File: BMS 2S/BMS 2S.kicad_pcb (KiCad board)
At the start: 2 copper layers, 20 parts

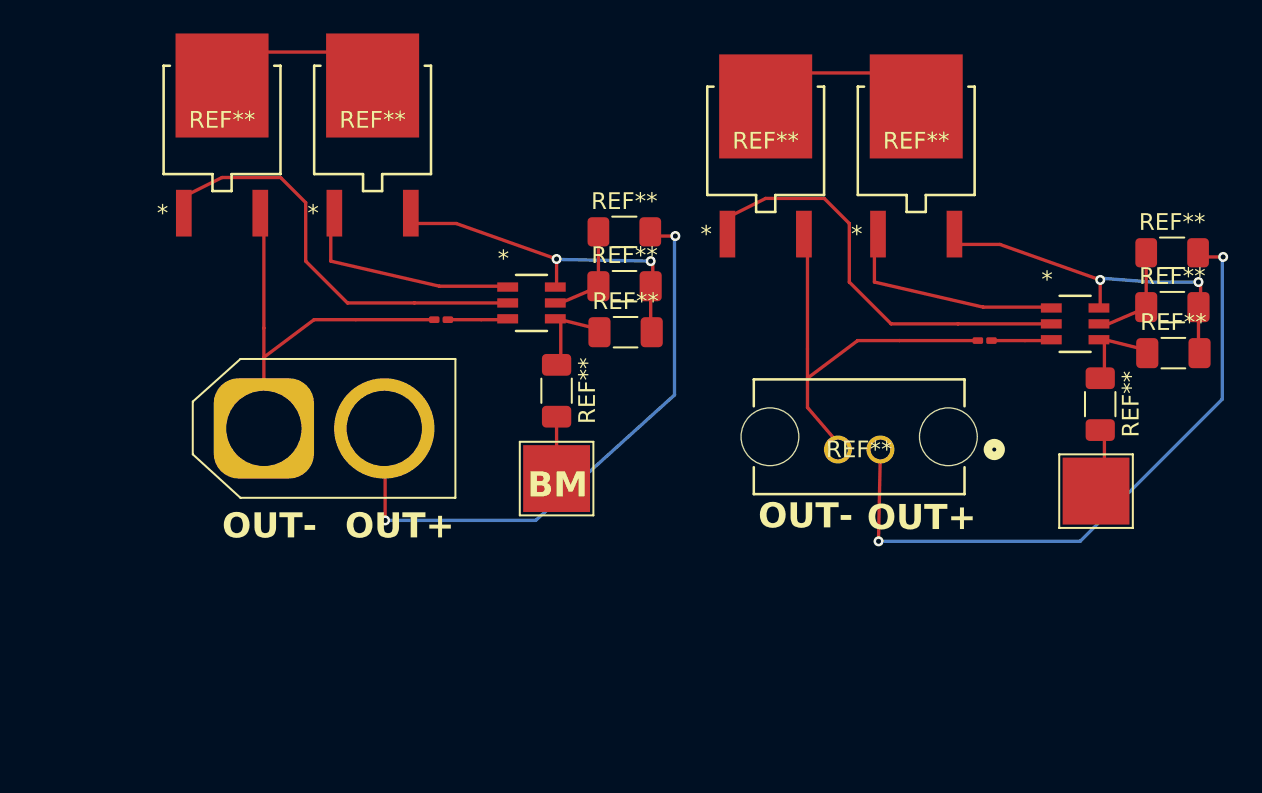
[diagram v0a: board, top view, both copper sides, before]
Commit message: Nouvelle itération du bms
Quelques bugs de connection a régler entre les power planes et les R,C et Screws terminals, + vérifications
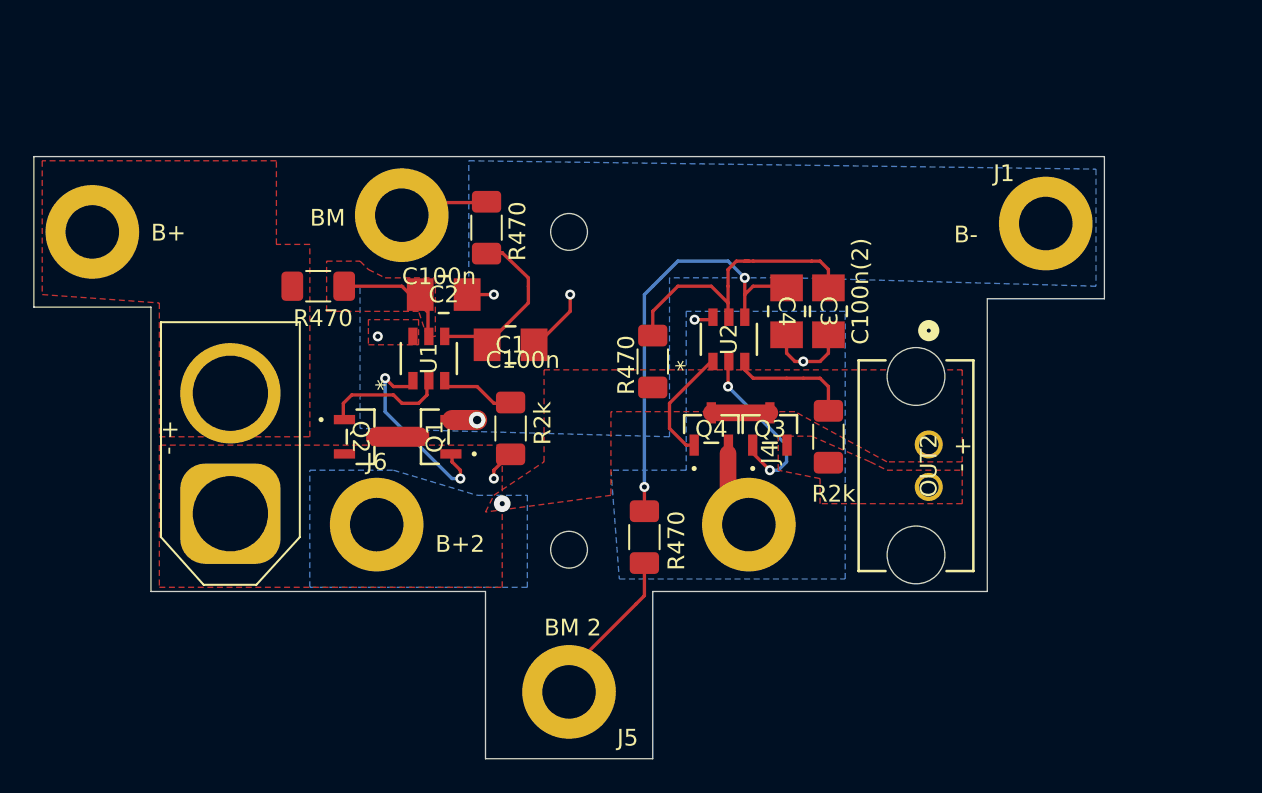
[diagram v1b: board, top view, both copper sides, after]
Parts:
- removed B+/-: AMASS_XT60-M_1x02_P7.20mm_Vertical, Connector_AMASS:AMASS_XT60-M_1x02_P7.20mm_Vertical
- removed the REF** at (142.1, 79.0)
- removed the REF** at (142.1, 85.0)
- removed the REF** at (136.2, 83.2)
- removed the REF** at (109.4, 83.8)
- removed the REF** at (137.8, 88.0)
- removed the REF** at (142.1, 82.2)
- removed the REF** at (85.2, 71.1)
- removed the REF** at (117.8, 72.3)
- removed the REF** at (94.2, 71.1)
- removed the REF** at (130.8, 84.2)
- removed the REF** at (105.2, 87.2)
- removed the REF** at (105.2, 92.5)
- removed the REF** at (137.5, 93.2)
- removed the REF** at (103.8, 82.0)
- removed the REF** at (109.3, 81.0)
- removed the REF** at (124.6, 90.8)
- removed the REF** at (109.3, 77.8)
- removed the REF** at (126.8, 72.3)
- removed the REF** at (98.3, 83.0)
- added C1: 1206cap, BMS_footprints:1206cap, F.Cu at (102.5, 84.5)
- added C2: 1206cap, BMS_footprints:1206cap, F.Cu at (98.5, 81.5)
- added C3: 1206cap, BMS_footprints:1206cap, F.Cu at (121.5, 82.5)
- added C4: 1206cap, BMS_footprints:1206cap, F.Cu at (119.0, 82.5)
- added J1: MountingHole_3.2mm_M3_DIN965_Pad, MountingHole:MountingHole_3.2mm_M3_DIN965_Pad, F.Cu at (134.5, 77.3)
- added J2: MountingHole_3.2mm_M3_DIN965_Pad, MountingHole:MountingHole_3.2mm_M3_DIN965_Pad, F.Cu at (96.0, 76.8)
- added J3: MountingHole_3.2mm_M3_DIN965_Pad, MountingHole:MountingHole_3.2mm_M3_DIN965_Pad, F.Cu at (77.5, 77.8)
- added J4: MountingHole_3.2mm_M3_DIN965_Pad, MountingHole:MountingHole_3.2mm_M3_DIN965_Pad, F.Cu at (116.7, 95.3)
- added J5: MountingHole_3.2mm_M3_DIN965_Pad, MountingHole:MountingHole_3.2mm_M3_DIN965_Pad, F.Cu at (106.0, 105.3)
- added J6: MountingHole_3.2mm_M3_DIN965_Pad, MountingHole:MountingHole_3.2mm_M3_DIN965_Pad, F.Cu at (94.5, 95.3)
- added OUT1: AMASS_XT60-M_1x02_P7.20mm_Vertical, Connector_AMASS:AMASS_XT60-M_1x02_P7.20mm_Vertical, F.Cu at (85.8, 94.6)
- added OUT2: 705450001, BMS_footprints:CONN_70545-xxxx_02_MOL, F.Cu at (127.5, 90.5)
- added Q1: DMG2302UK-7, BMS_footprints:SOT23_DMG230_DIO, F.Cu at (98.0, 90.0)
- added Q2: DMG2302UK-7, BMS_footprints:SOT23_DMG230_DIO, F.Cu at (93.5, 90.0)
- added Q3: DMG2302UK-7, BMS_footprints:SOT23_DMG230_DIO, F.Cu at (118.0, 89.5)
- added Q4: DMG2302UK-7, BMS_footprints:SOT23_DMG230_DIO, F.Cu at (114.5, 89.5)
- added R1: R_1206_3216Metric_Pad1.30x1.75mm_HandSolder, Resistor_SMD:R_1206_3216Metric_Pad1.30x1.75mm_HandSolder, F.Cu at (101.1, 77.5)
- added R2: R_1206_3216Metric_Pad1.30x1.75mm_HandSolder, Resistor_SMD:R_1206_3216Metric_Pad1.30x1.75mm_HandSolder, F.Cu at (91.0, 81.0)
- added R3: R_1206_3216Metric_Pad1.30x1.75mm_HandSolder, Resistor_SMD:R_1206_3216Metric_Pad1.30x1.75mm_HandSolder, F.Cu at (102.5, 89.5)
- added R4: R_1206_3216Metric_Pad1.30x1.75mm_HandSolder, Resistor_SMD:R_1206_3216Metric_Pad1.30x1.75mm_HandSolder, F.Cu at (111.0, 85.5)
- added R5: R_1206_3216Metric_Pad1.30x1.75mm_HandSolder, Resistor_SMD:R_1206_3216Metric_Pad1.30x1.75mm_HandSolder, F.Cu at (110.5, 96.0)
- added R6: R_1206_3216Metric_Pad1.30x1.75mm_HandSolder, Resistor_SMD:R_1206_3216Metric_Pad1.30x1.75mm_HandSolder, F.Cu at (121.5, 90.0)
- added REF**: MountingHole_2.2mm_M2, MountingHole:MountingHole_2.2mm_M2, F.Cu at (106.0, 77.8)
- added REF**: MountingHole_2.2mm_M2, MountingHole:MountingHole_2.2mm_M2, F.Cu at (106.0, 96.8)
- added U1: S-8252AAZ-M6T1U, BMS_footprints:SOT236-A-PKG_MP006-A-P-SD-2.1_ABL, F.Cu at (97.6, 85.3)
- added U2: S-8252AAZ-M6T1U, BMS_footprints:SOT236-A-PKG_MP006-A-P-SD-2.1_ABL, F.Cu at (115.5, 84.2)
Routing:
- net Net-(U2-VC): vias 0 -> 2
- net Net-(Q3-G): vias 0 -> 2
- net Net-(Q1-G): vias 0 -> 2
- net B-2: vias 0 -> 1
- net B-: vias 0 -> 2
- net (no net): vias 8 -> 5
- added copper zone on F.Cu, net (none)
- added copper zone on B.Cu, net B-
- added copper zone on F.Cu, net B-
- added copper zone on B.Cu, net B-2
- added copper zone on F.Cu, net Net-(U1-VDD)
- added copper zone on B.Cu, net Out+ B+2
- added copper zone on F.Cu, net Out+ B+2
- added copper zone on F.Cu, net Out-
- added copper zone on F.Cu, net Out-2
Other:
- board outline added: 64 x 36 mm
- board text added: "+ -"
- board text added: "B+"
- board text added: "B+2"
- board text added: "B-"
- board text added: "BM 2"
- board text added: "C100n"
- board text added: "C100n(2)"
- board text added: "R2k"
- board text added: "R470"
- board text removed: "OUT+"
- board text removed: "OUT-"
- board text removed: "gnd"

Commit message: BMS- Réglage des bugs de link power plane
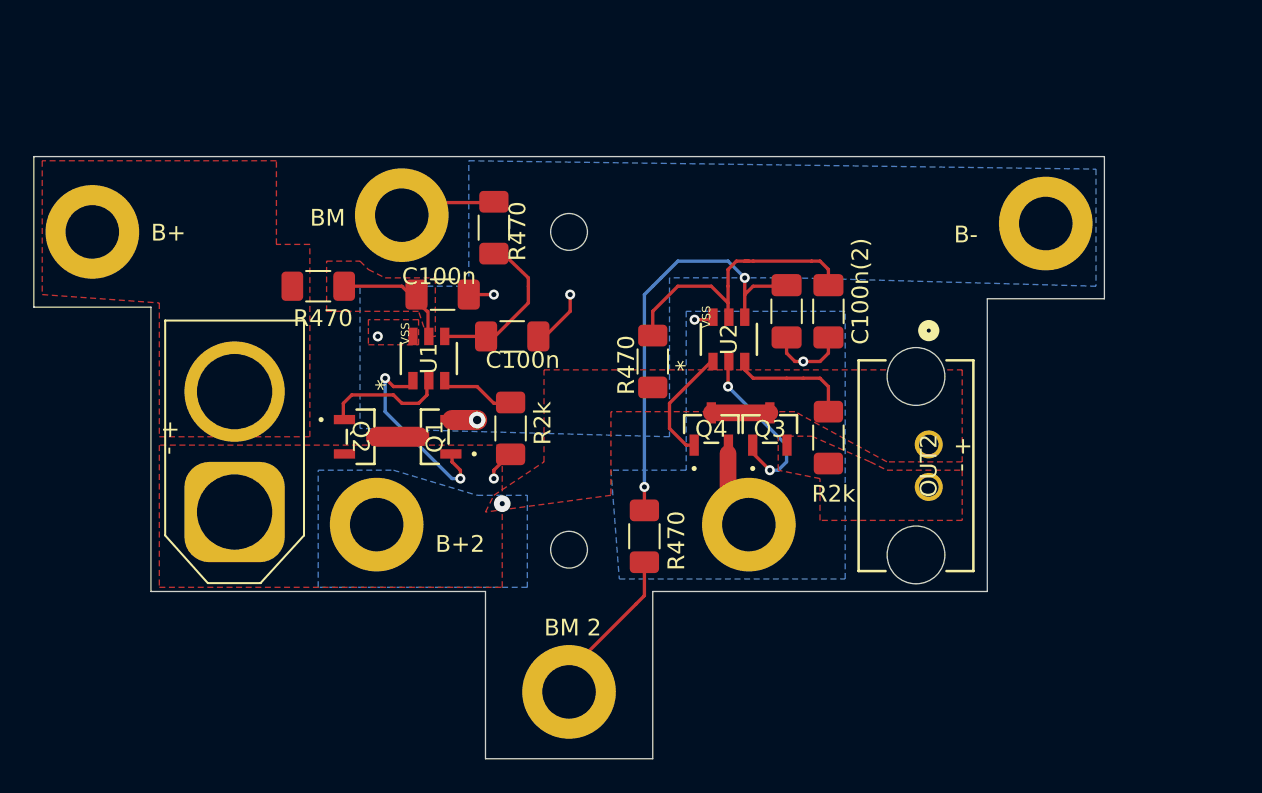
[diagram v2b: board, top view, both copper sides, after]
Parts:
- C1, C2, C3, C4: value 1206cap -> 100n; footprint BMS_footprints:1206cap -> Capacitor_SMD:C_1206_3216Metric_Pad1.33x1.80mm_HandSolder
- J1, J2, J3, J4, J5, J6: value MountingHole_3.2mm_M3_DIN965_Pad -> Screw_Terminal_01x01
- OUT1: value AMASS_XT60-M_1x02_P7.20mm_Vertical -> XT60
- R1, R2, R4, R5: value R_1206_3216Metric_Pad1.30x1.75mm_HandSolder -> 470
- R3, R6: value R_1206_3216Metric_Pad1.30x1.75mm_HandSolder -> 2k
- moved C1 0.51 mm to (102.6, 84.0)
- moved R1 0.44 mm to (101.5, 77.5)
- moved OUT1 0.27 mm to (86.0, 94.5)
- moved C2 0.06 mm to (98.4, 81.5)
- turned R6 to 90 degrees
- turned R2 to 180 degrees
- turned R3 to 90 degrees
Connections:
- C1 pad 1: (no net) -> Net-(U1-VC)
- C1 pad 2: (no net) -> B-
- C2 pad 1: (no net) -> Net-(U1-VDD)
- C2 pad 2: (no net) -> B-
- C3 pad 1: (no net) -> Net-(U2-VDD)
- C3 pad 2: (no net) -> B-2
- C4 pad 1: (no net) -> Net-(U2-VC)
- C4 pad 2: (no net) -> B-2
- J1 pad 1: (no net) -> B-
- J2 pad 1: (no net) -> BM
- J3 pad 1: (no net) -> Out+ B+
- J4 pad 1: (no net) -> B-2
- J5 pad 1: (no net) -> BM2
- J6 pad 1: (no net) -> Out+ B+2
- OUT1 pad 1: (no net) -> Out-
- OUT1 pad 2: (no net) -> Out+ B+
- R1 pad 1: (no net) -> Net-(U1-VC)
- R1 pad 2: (no net) -> BM
- R2 pad 1: (no net) -> Net-(U1-VDD)
- R2 pad 2: (no net) -> Out+ B+
- R3 pad 1: (no net) -> Out-
- R3 pad 2: (no net) -> Net-(U1-VM)
- R4 pad 1: (no net) -> Net-(U2-VDD)
- R4 pad 2: (no net) -> Out+ B+2
- R5 pad 1: (no net) -> Net-(U2-VC)
- R5 pad 2: (no net) -> BM2
- R6 pad 1: (no net) -> Out-2
- R6 pad 2: (no net) -> Net-(U2-VM)
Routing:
- net Out-: vias 0 -> 1
- net Out+ B+2: vias 0 -> 1
- net B-2: vias 1 -> 2
- net B-: vias 2 -> 4
- net (no net): vias 5 -> 0
- added copper zone on F.Cu, net Out+ B+
- removed copper zone on F.Cu, net (none)
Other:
- board text added: "VSS"
